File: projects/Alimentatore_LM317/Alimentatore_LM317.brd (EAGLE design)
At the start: 65.4 x 99.4 mm, 19 parts

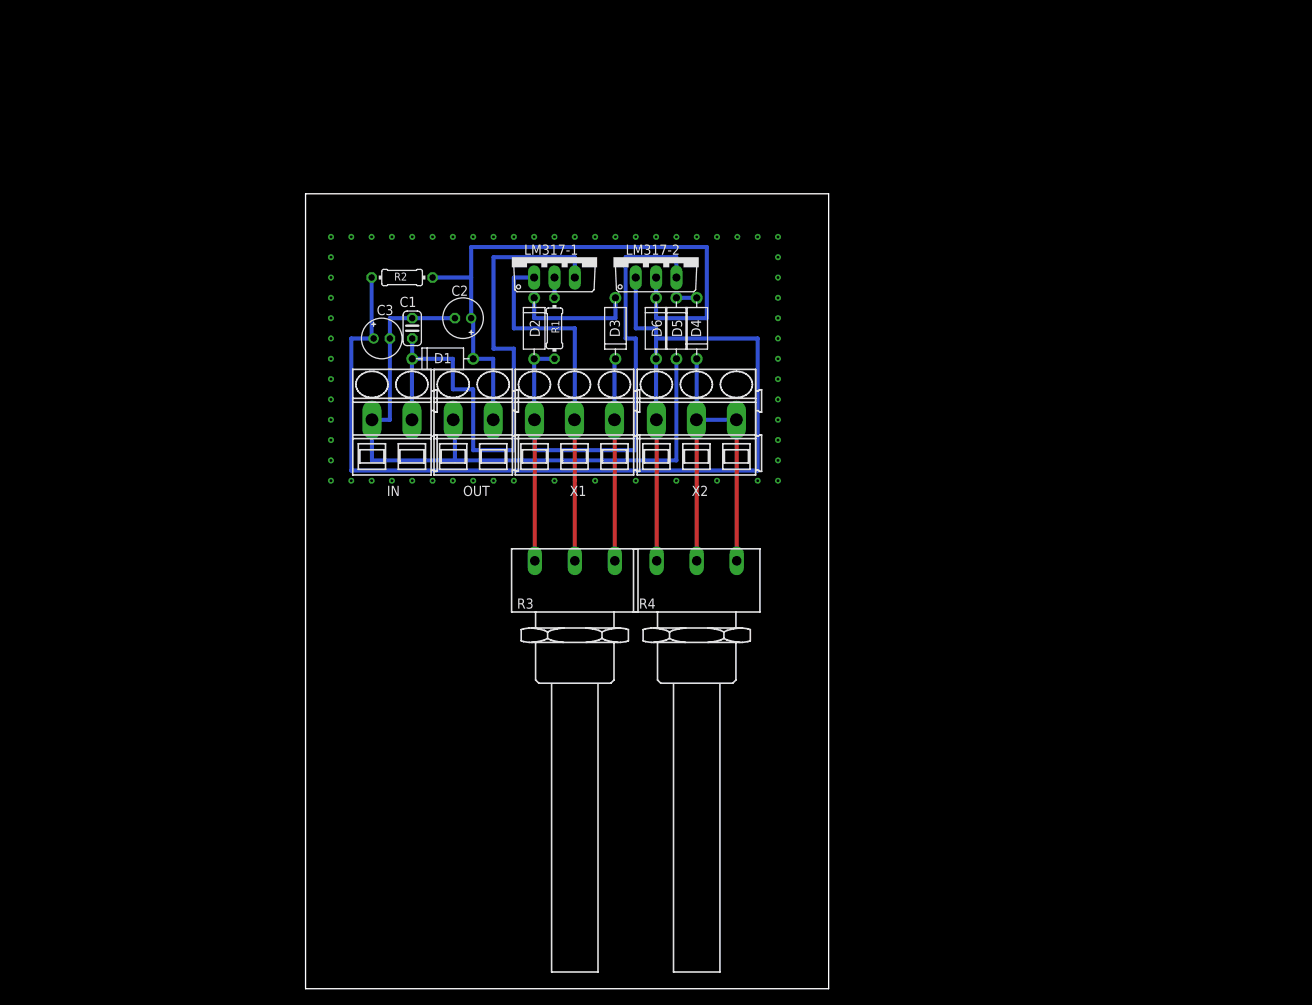
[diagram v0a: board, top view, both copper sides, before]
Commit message: aggiunti circuiti alternativi LM317.
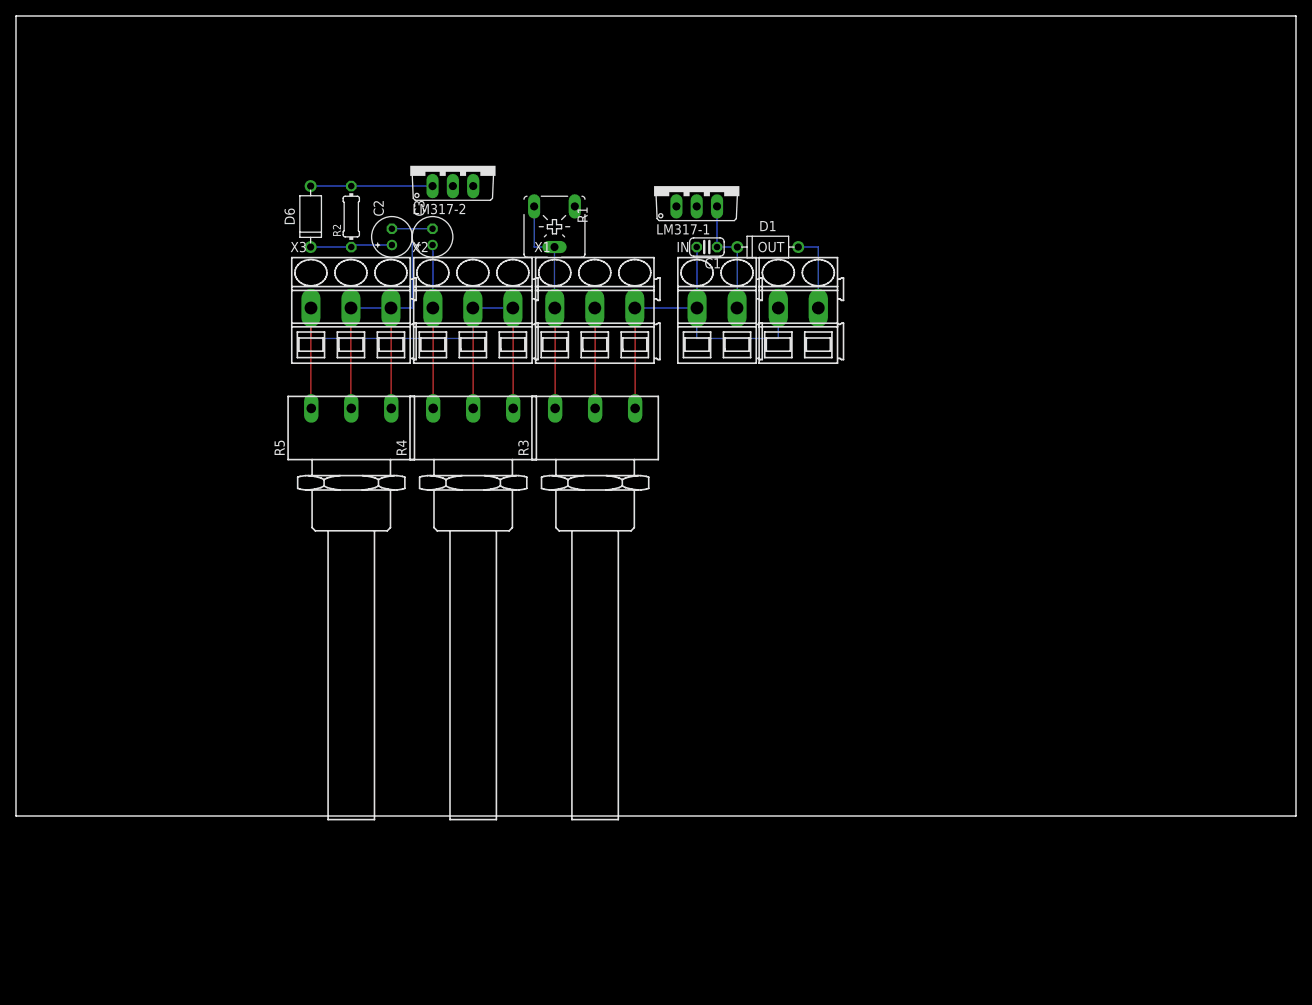
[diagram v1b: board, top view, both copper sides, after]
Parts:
- removed D2, D3, D4, D5: 1N4001, diode_MOD:DIOAD860W70L460D235B
- added R5: 1k, piher:PC16S
- added X3: (no value), con-phoenix-smkdsp:SMKDSP_1,5/3
- R1: value (none) -> 500; device rcl:0204/7 -> pot:CA6V
- moved D6 45.4 mm to (36.8, 74.9), turned to 90 degrees
- moved OUT 43.0 mm to (97.8, 63.5)
- moved D1 43.0 mm to (94.0, 71.1)
- moved IN 43.0 mm to (87.6, 63.5)
- moved C1 38.2 mm to (86.4, 71.1), turned to 180 degrees
- moved R4 33.8 mm to (57.1, 44.5)
- moved X2 31.2 mm to (54.6, 63.5)
- moved LM317-2 27.9 mm to (54.6, 81.3)
- moved LM317-1 19.9 mm to (85.1, 78.7)
- moved R3 19.2 mm to (72.4, 44.5)
- moved C3 14.2 mm to (52.1, 72.4), turned to 90 degrees
- moved X1 14.2 mm to (69.8, 63.5)
- moved C2 13.5 mm to (47.0, 72.4), turned to 90 degrees
- moved R1 12.7 mm to (67.3, 73.7), turned to 180 degrees
- moved R2 9.92 mm to (41.9, 74.9), turned to 90 degrees
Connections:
- removed net N$10: D4.1, R4.1E, R4.1S, X2.2, X2.3
- removed net N$6: D4.2, D5.1
- removed net N$7: D3.1, R3.1E, X1.3
- net GND: now also R3.1E, R5.1E, R5.1S, X1.3, X3.2, X3.3; no longer D5.2
- net N$2: now also R1.A; no longer R1.2
- net N$3: now also R1.E, R1.S; no longer D2.2, R1.1
- net N$4: now also R4.1E, R4.1S, R5.1A, X2.2, X2.3, X3.1; no longer D2.1, D3.2
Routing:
- net N$9: track 145.2 -> 35.8 mm
- net N$1: track 79.0 -> 20.5 mm
- net VCC: track 73.7 -> 15.3 mm
- net N$4: track 15.2 -> 70.7 mm
- net N$3: track 78.6 -> 27.8 mm
- net N$10: track 48.0 -> 0.00 mm, vias 1 -> 0
- net N$5: track 45.6 -> 12.6 mm
- net N$7: track 25.4 -> 0.00 mm
- net GND: track 84.3 -> 93.6 mm
- net N$6: track 2.54 -> 0.00 mm
- net N$2: track 2.54 -> 0.00 mm
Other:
- board size 65.4 x 99.4 mm -> 160 x 100 mm
